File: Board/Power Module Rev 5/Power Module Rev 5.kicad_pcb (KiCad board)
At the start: 4 copper layers, 76.2 x 82.6 mm, 153 parts, among them J1 9-6437287-8, J2 Conn_ARM_SWD_TagConnect_TC203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, J3 Conn_01x16_Pin, J4 USB_C_Receptacle_USB2.0, U1 AP2112K-3.3, U10 BTS7002-1EPP, U11 MCP2558FD-xMF, U12 BTS7008-2EPA, U13 BTS7008-2EPA, U14 TPS2116DRLR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

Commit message: Board Update
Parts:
- added G***: LOGO, Bryan_Lib:Brytec_Logo, B.Cu at (159.3, 88.8)
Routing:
- net GND: vias 99 -> 107
- net +12V: vias 25 -> 28
- added copper zone on B.Cu, net GND
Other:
- board text added: "BOOT_0"
- board text added: "Power Module - Rev 5 2023"
- board text added: "RESET"

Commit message: Board Update
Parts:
- added D2: LED_Small, LED_SMD:LED_0603_1608Metric_Pad1.05x0.95mm_HandSolder, F.Cu at (121.2, 53.4)
- added R68: 65, Resistor_SMD:R_0603_1608Metric_Pad0.98x0.95mm_HandSolder, F.Cu at (119.8, 53.4)
- J3: footprint Eagle_WP-BUCF (rev22a):WP-BUFU_7461147_HAL -> Eagle_WP-BUCF (rev22a):WP-BUFU_7461097_HAL
- moved C34 0.41 mm to (115.0, 97.6)
- moved C36 0.41 mm to (107.7, 97.6)
- moved R1 0.41 mm to (116.4, 97.6)
- moved R15 0.41 mm to (109.1, 97.6)
- moved R26 0.41 mm to (117.9, 97.6)
- moved R27 0.41 mm to (110.6, 97.6)
- moved R32 0.41 mm to (119.4, 97.6)
- moved R33 0.41 mm to (112.0, 97.6)
- moved R38 0.41 mm to (120.8, 97.6)
- moved R39 0.41 mm to (113.5, 97.6)
- moved R34 0.38 mm to (137.6, 97.6)
- moved R40 0.38 mm to (139.0, 97.6)
- moved C25 0.38 mm to (146.4, 97.6)
- moved C37 0.38 mm to (133.2, 97.6)
- moved R16 0.38 mm to (134.6, 97.6)
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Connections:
- net /Mcu/SPI1_SS2 renamed /Mcu/SPI1_SS_Memory
- net Power Switch Status renamed PowerSwitchStatus
- net SPI1_SS1 renamed SPI1_SS_L9966
- U17 pad 22: unconnected-(U17-PB10-Pad22) -> /Mcu/User_Led
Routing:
- net /Mcu/User_Led: track 0.00 -> 11.4 mm
- net Net-(D2-A): track 0.00 -> 2.38 mm
- net GND: track 139.1 -> 141.2 mm, vias 107 -> 108
- net +12V: track 47.6 -> 48.6 mm
- net /High Side Drivers/Den4: track 22.6 -> 23.4 mm
- net /High Side Drivers/In6: track 6.54 -> 5.90 mm
- net Net-(U10-IN): track 3.97 -> 4.58 mm
- net Net-(U10-GND): track 4.76 -> 5.36 mm
- net Net-(U3-DEN): track 4.66 -> 5.24 mm
- net Net-(U3-IS): track 52.4 -> 52.9 mm
- net Net-(U10-DEN): track 3.18 -> 3.72 mm
- net Net-(U9-IS): track 50.1 -> 50.6 mm

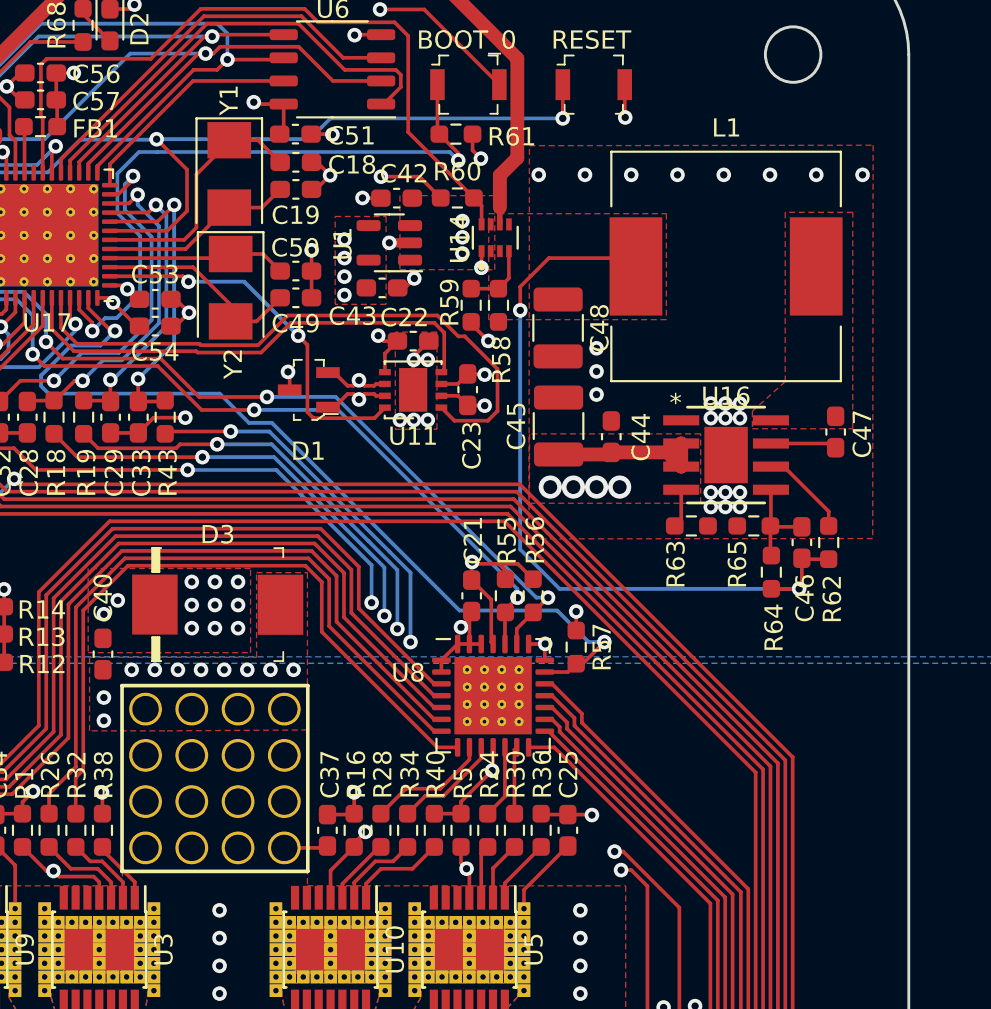
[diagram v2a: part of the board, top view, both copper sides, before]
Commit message: Board - changed regulator
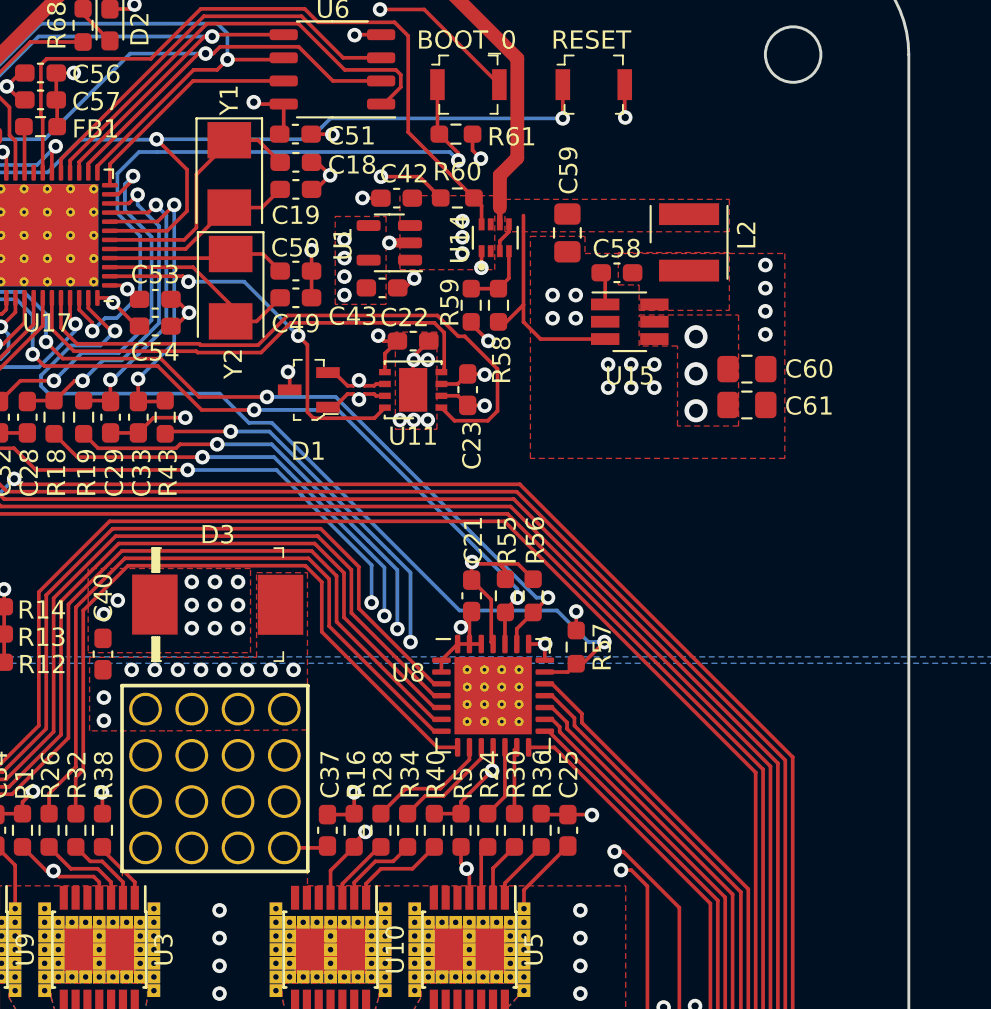
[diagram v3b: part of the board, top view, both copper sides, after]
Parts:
- removed C44, C47: 100nF, Capacitor_SMD:C_0603_1608Metric_Pad1.08x0.95mm_HandSolder
- removed C45: 4.7uF, Capacitor_SMD:C_1210_3225Metric_Pad1.33x2.70mm_HandSolder
- removed C46: 39pF, Capacitor_SMD:C_0603_1608Metric_Pad1.08x0.95mm_HandSolder
- removed C48: 47uF, Capacitor_SMD:C_1210_3225Metric_Pad1.33x2.70mm_HandSolder
- removed L1: 39uH, Inductor_SMD:L_Wuerth_WE-PD-Typ-LS
- removed R62: 100k, Resistor_SMD:R_0603_1608Metric_Pad0.98x0.95mm_HandSolder
- removed R63: 64.9k, Resistor_SMD:R_0603_1608Metric_Pad0.98x0.95mm_HandSolder
- removed R64: 40.2k, Resistor_SMD:R_0603_1608Metric_Pad0.98x0.95mm_HandSolder
- removed R65: 10k, Resistor_SMD:R_0603_1608Metric_Pad0.98x0.95mm_HandSolder
- removed U16: PLMR38010FSQDDARQ1, MyKiCadLibraries:HSOP8_DDA_TEX
- added C58: 100nF, Capacitor_SMD:C_0603_1608Metric_Pad1.08x0.95mm_HandSolder, F.Cu at (149.1, 67.0)
- added C59: 10uF, Capacitor_SMD:C_0805_2012Metric_Pad1.18x1.45mm_HandSolder, F.Cu at (146.4, 64.8)
- added C60: 100nF, Capacitor_SMD:C_0805_2012Metric_Pad1.18x1.45mm_HandSolder, F.Cu at (156.2, 72.3)
- added C61: 4.7uF, Capacitor_SMD:C_0805_2012Metric_Pad1.18x1.45mm_HandSolder, F.Cu at (156.2, 74.2)
- added L2: 6.8uH, Inductor_SMD_Wurth:L_Wurth_WE-LQSH-4020, F.Cu at (153.0, 65.3)
- added U15: ~, Package_TO_SOT_SMD:SOT-23-6_Handsoldering, F.Cu at (149.8, 69.7)
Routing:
- net Regulated 5V: track 42.6 -> 14.2 mm, vias 2 -> 0
- net Net-(U16-fb): track 5.40 -> 0.00 mm
- net Net-(U16-pg): track 4.99 -> 0.00 mm
- net Net-(U16-boot): track 3.65 -> 0.00 mm
- net Ignition: track 60.6 -> 62.9 mm, vias 4 -> 3
- net Net-(U16-rt/sync): track 2.13 -> 0.00 mm
- net Net-(U15-CB): track 0.00 -> 1.83 mm
- net GND: vias 108 -> 99
- added copper zone on F.Cu, net Net-(U15-SW)
- removed copper zone on F.Cu, net Net-(U16-sw)

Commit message: Board Update and Gerbers
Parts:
- removed Y1: Crystal_Small, Crystal:Crystal_SMD_5032-2Pin_5.0x3.2mm
- added Y3: 8MHz, Crystal:Crystal_SMD_5032-4Pin_5.0x3.2mm, F.Cu at (128.5, 61.6)
- C18, C19, C49, C50: value ~ -> 10pF
- C2, C24, C25, C26, C3, C34, C36, C37, C38, C39, C40, C41, C5, C58, C60: value 100nF -> 0.1uF
- G***: moved to F.Cu
- R55, R56: value 4K7 -> 4.7K
- R58, R59, R60: value R_Small -> 10K
- U15: value ~ -> LMR50410Y5FQDBVRQ1
- Y2: value Crystal_Small -> 32.768kHz; footprint Crystal:Crystal_SMD_5032-2Pin_5.0x3.2mm -> Crystal:Crystal_SMD_3215-2Pin_3.2x1.5mm
- moved G*** 4.09 mm to (161.0, 92.5), turned to -90 degrees
- moved Y2 0.91 mm to (127.9, 66.9), turned to 90 degrees
- moved C18 0.79 mm to (132.2, 60.9)
- moved C19 0.79 mm to (132.2, 62.4)
- moved C51 0.79 mm to (132.2, 59.3)
- moved C49 0.76 mm to (131.4, 67.6)
- moved C50 0.76 mm to (131.4, 66.1)
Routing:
- net GND: track 141.2 -> 145.5 mm, vias 99 -> 101
- net Net-(U17-PC14): track 11.6 -> 10.2 mm
- net Net-(U17-PF0): track 10.7 -> 11.5 mm
- net Net-(U17-PF1): track 13.8 -> 14.6 mm

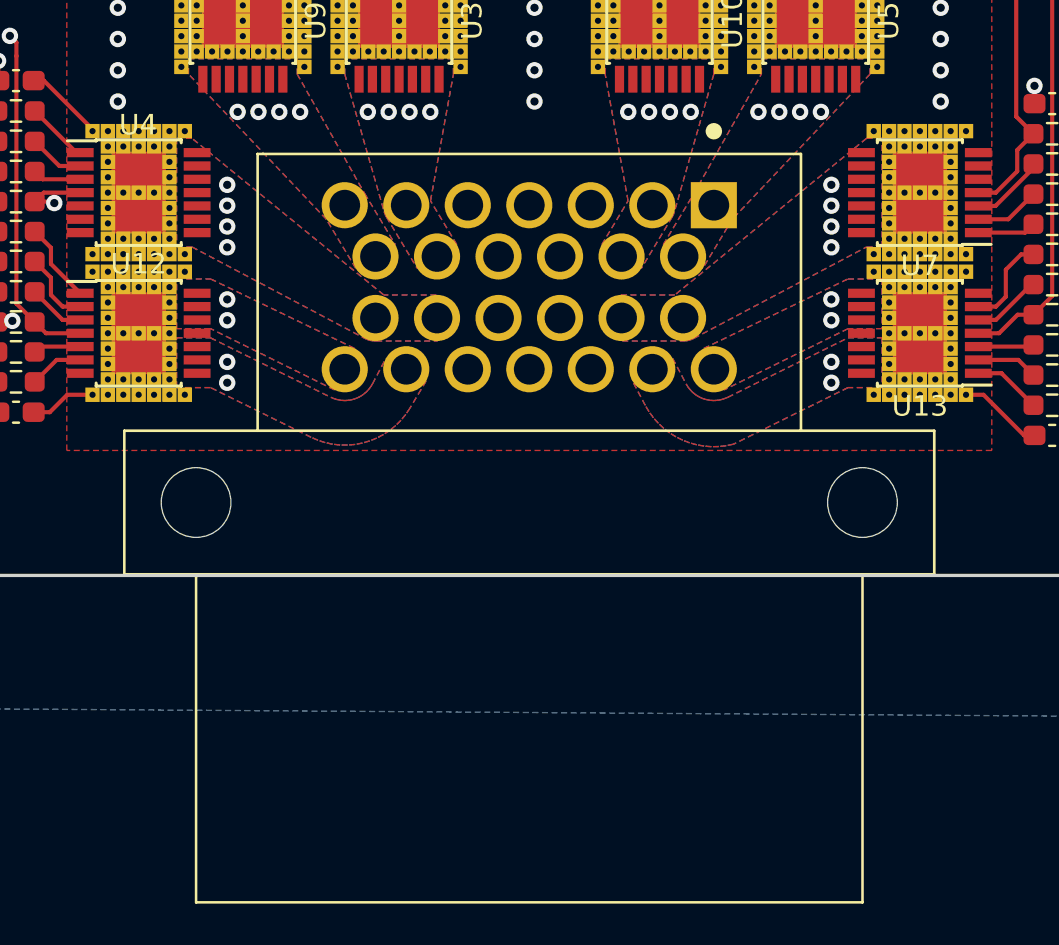
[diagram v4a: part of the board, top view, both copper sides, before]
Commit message: Board - fixed connector pin numbering
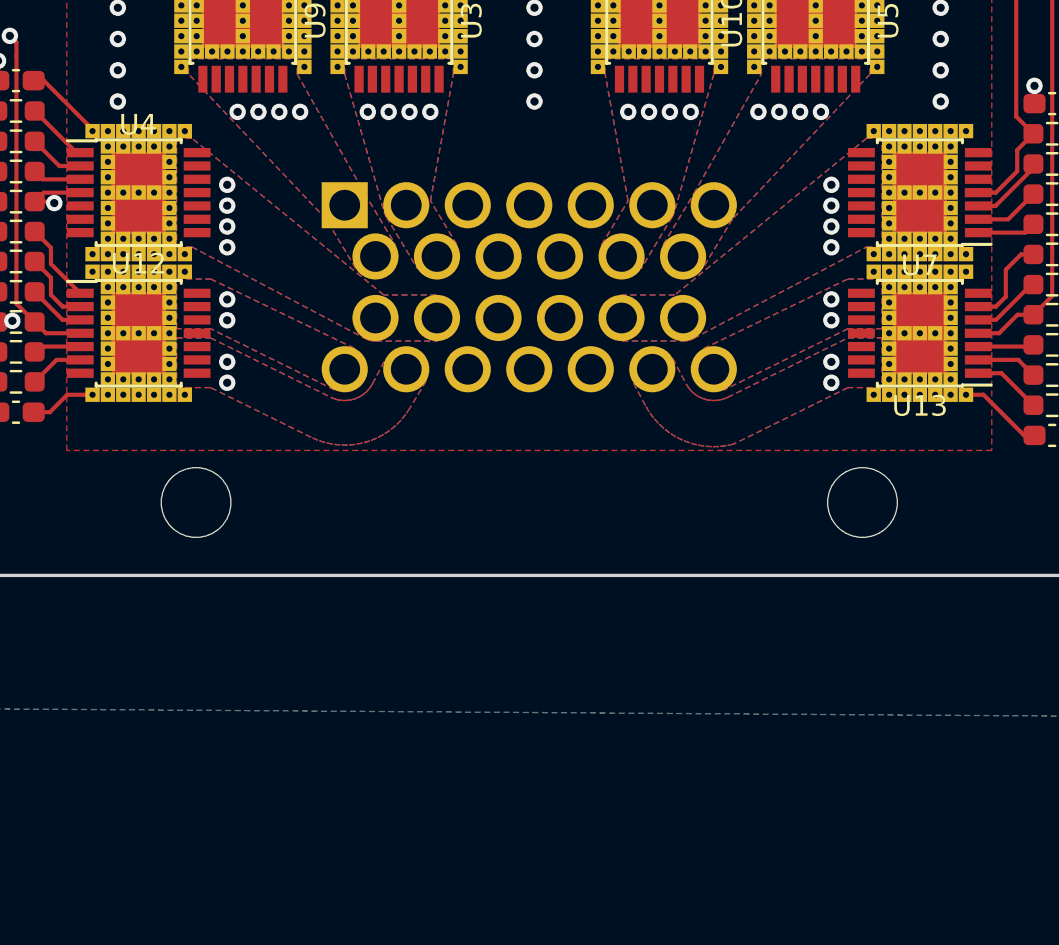
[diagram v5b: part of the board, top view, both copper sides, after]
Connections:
- J1 pad 1: Output3 -> Output5
- J1 pad 10: +5V -> GND
- J1 pad 11: GND -> +5V
- J1 pad 12: Output1 -> Output6
- J1 pad 13: Output5 -> Output3
- J1 pad 14: Output4 -> Output2
- J1 pad 15: Output4 -> Output2
- J1 pad 18: Output2 -> Output4
- J1 pad 19: Output2 -> Output4
- J1 pad 2: Output6 -> Output1
- J1 pad 20: Output10 -> Output7
- J1 pad 21: Output9 -> Output8
- J1 pad 22: Input1 -> Input3
- J1 pad 24: Input3 -> Input1
- J1 pad 25: Output8 -> Output9
- J1 pad 26: Output7 -> Output10
- J1 pad 3: Ignition -> Can-
- J1 pad 5: Can- -> Ignition
- J1 pad 6: Output1 -> Output6
- J1 pad 7: Output5 -> Output3
- J1 pad 8: Output3 -> Output5
- J1 pad 9: Output6 -> Output1
